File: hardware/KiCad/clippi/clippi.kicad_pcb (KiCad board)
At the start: 2 copper layers, 65 x 56 mm, 23 parts, among them J1 GPIO, J2 Conn_01x16_Pin, Q1 BSS138

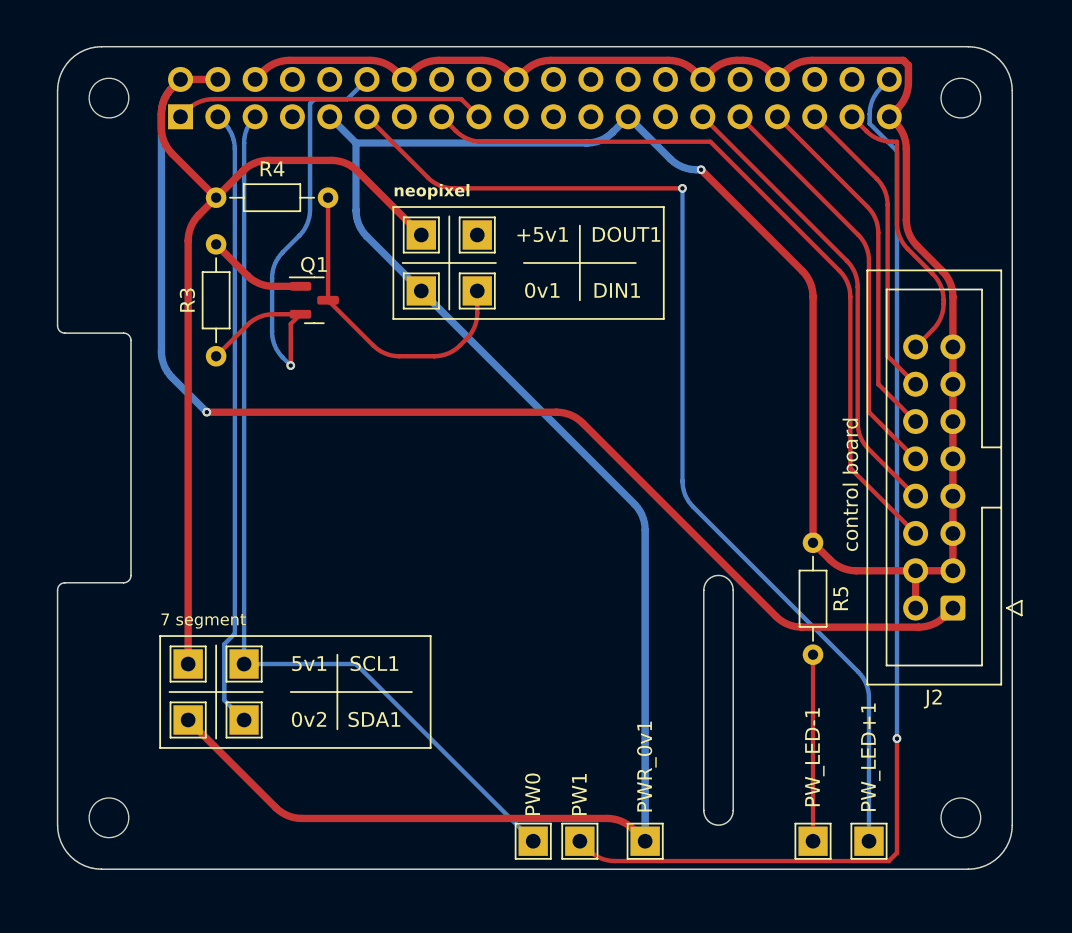
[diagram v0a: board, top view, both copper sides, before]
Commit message: re-lay out the pi hat, re-trace, add copper fill, and I generated gerber files and set it off to PCB way
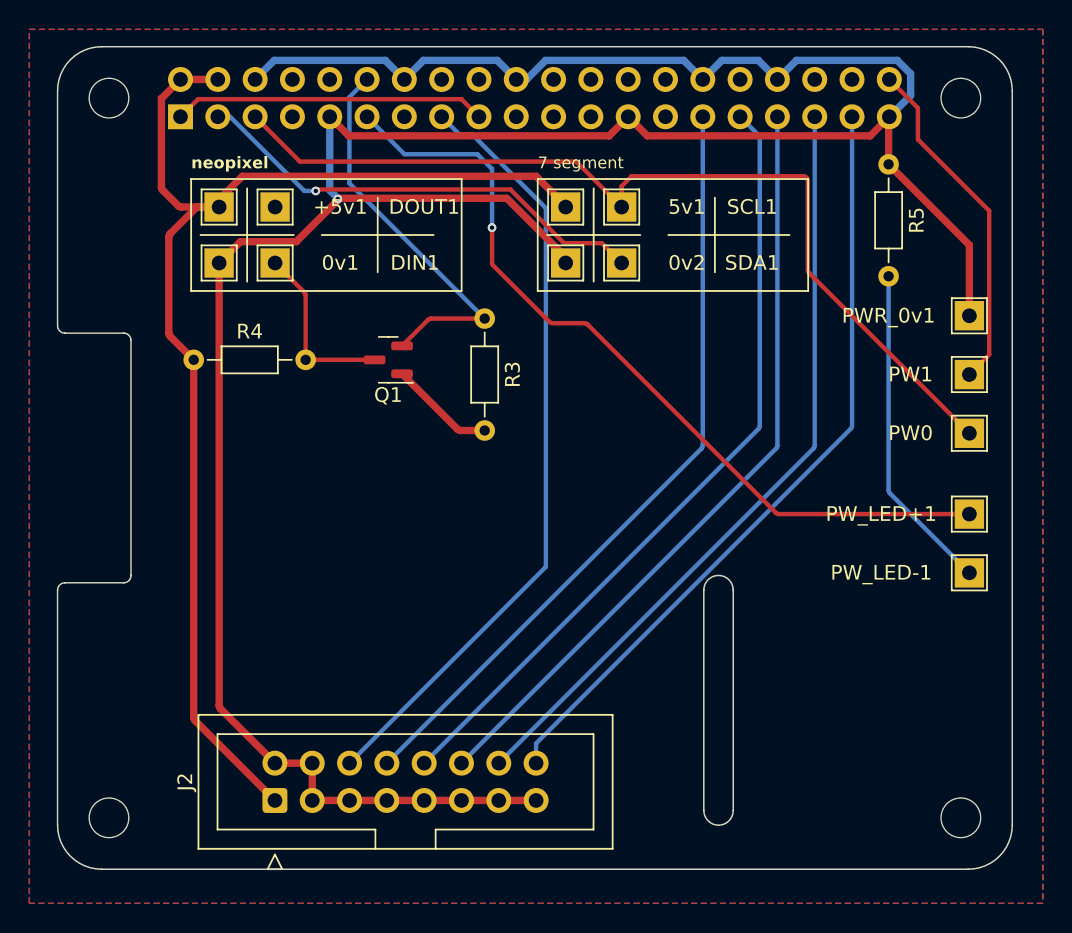
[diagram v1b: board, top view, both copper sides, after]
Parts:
- moved J2 48.0 mm to (114.8, 95.3), turned to 90 degrees
- moved PWR_0v1 42.0 mm to (162.1, 62.3)
- moved PW1 41.4 mm to (162.1, 66.3)
- moved PW0 40.7 mm to (162.1, 70.3)
- moved 0v2 40.4 mm to (134.6, 58.7)
- moved 5v1 40.4 mm to (134.6, 54.9)
- moved SCL1 40.4 mm to (138.4, 54.9)
- moved SDA1 40.4 mm to (138.4, 58.7)
- moved R5 26.3 mm to (156.6, 52.0)
- moved PW_LED+1 23.3 mm to (162.1, 75.8)
- moved PW_LED-1 21.1 mm to (162.1, 79.8)
- moved R3 18.5 mm to (129.1, 62.5), turned to -90 degrees
- moved +5v1 13.9 mm to (111.0, 54.9)
- moved 0v1 13.9 mm to (111.0, 58.7)
- moved DIN1 13.9 mm to (114.8, 58.7)
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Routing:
- net +5V: track 143.0 -> 86.3 mm, vias 1 -> 0
- net /GPIO21/PCM.DOUT: track 76.1 -> 23.5 mm, vias 1 -> 0
- net GND: track 243.6 -> 198.7 mm
- net /GPIO26: track 19.4 -> 52.9 mm
- net /GPIO19/PCM.FS: track 20.9 -> 52.9 mm
- net /GPIO13/PWM1: track 24.5 -> 52.9 mm
- net /GPIO6: track 28.1 -> 54.0 mm
- net /GPIO5: track 31.6 -> 52.9 mm
- net /GPIO17: track 72.8 -> 56.0 mm
- net /GPIO2/SDA1: track 42.3 -> 31.7 mm, vias 0 -> 1
- net Net-(PW_LED-1-Pin_1): track 12.7 -> 22.5 mm
- net /NPIXEL_DATA_IN: track 21.7 -> 12.1 mm
- net /GPIO18/PCM.CLK: track 34.2 -> 27.0 mm, vias 1 -> 0
- net /GPIO22: track 51.2 -> 53.0 mm
- net /GPIO3/SCL1: track 62.1 -> 63.8 mm
- added copper zone on B.Cu, net GND
- added copper zone on F.Cu, net GND
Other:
- board text removed: "control board"

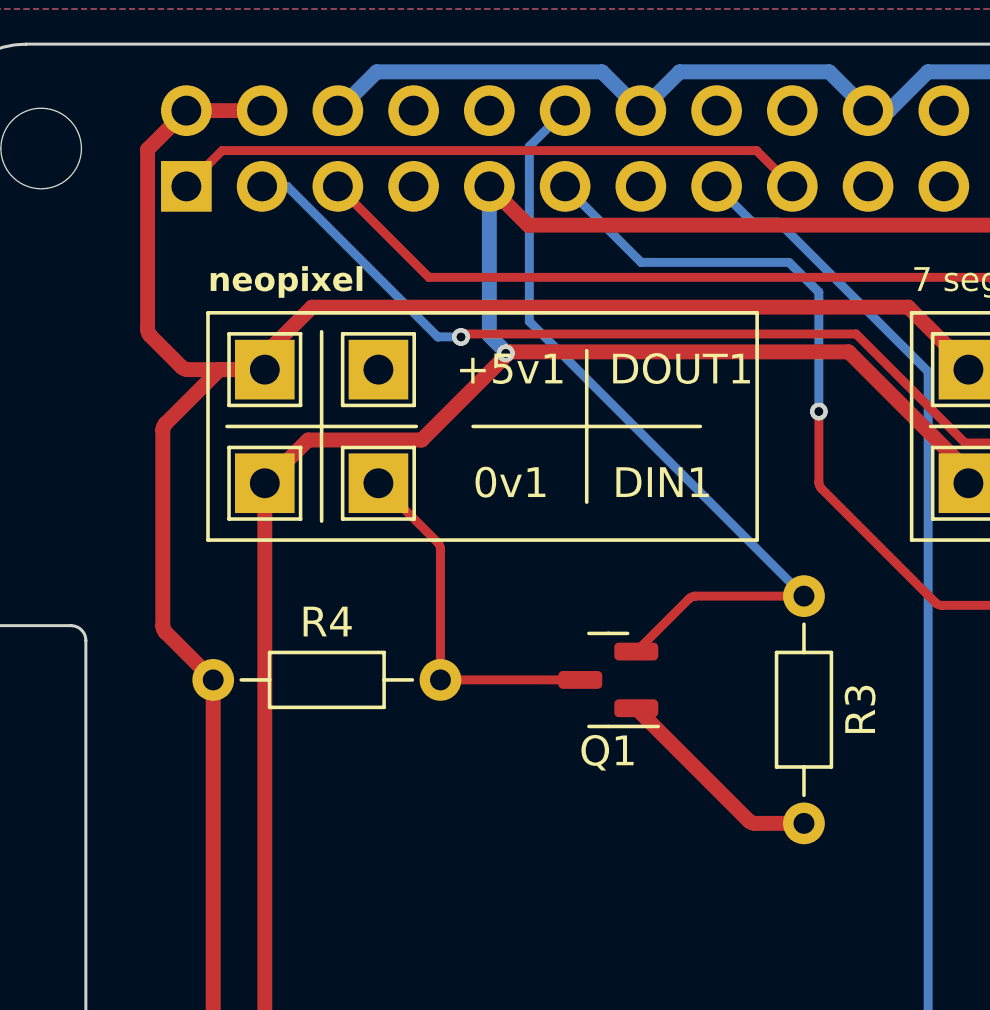
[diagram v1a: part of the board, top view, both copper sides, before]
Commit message: fix pi hat board/schematic to ensure 3.3v is supplied to the logic shifter, that got missed
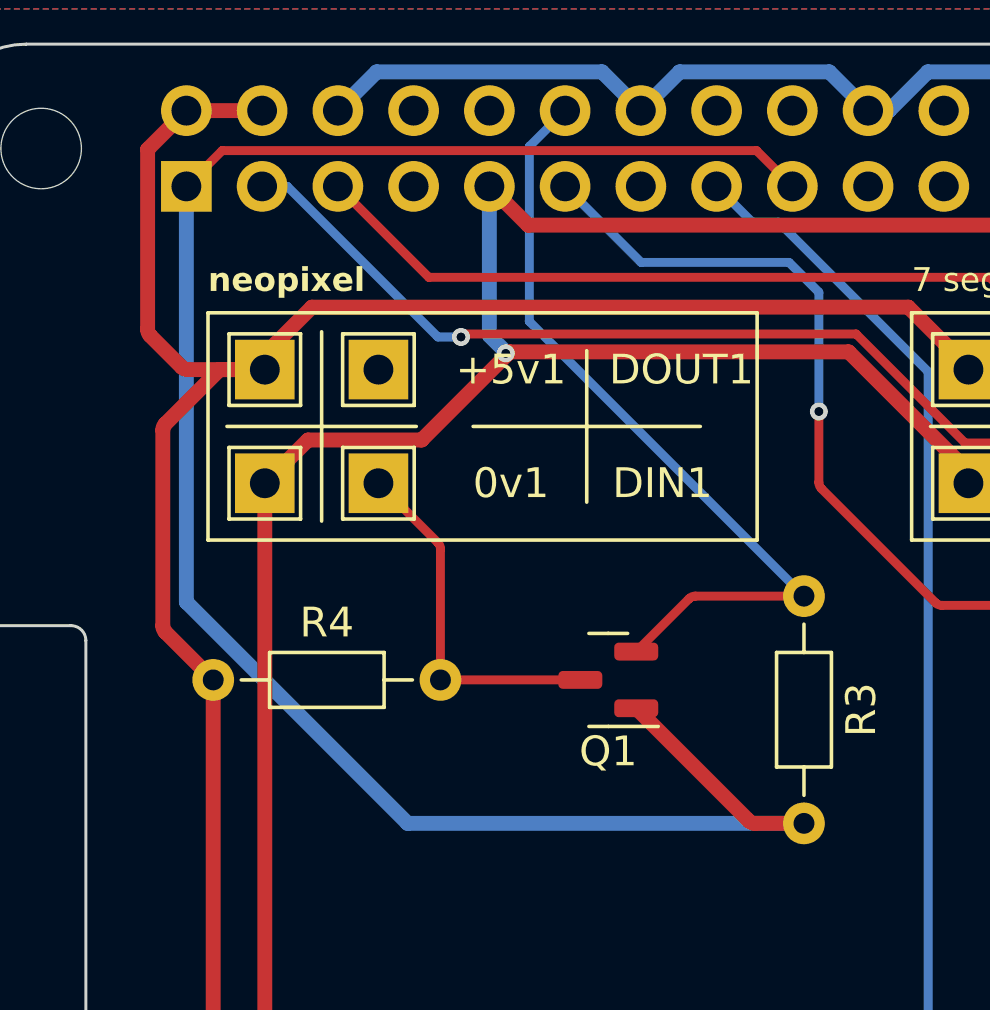
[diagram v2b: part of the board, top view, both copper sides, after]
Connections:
- Q1 pad 1: +3.3V -> +3V3
- R3 pad 2: +3.3V -> +3V3
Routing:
- net +3V3: track 21.3 -> 66.2 mm
- net +3.3V: track 7.21 -> 0.00 mm
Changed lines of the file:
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@@
   (net 33 "/NPIXEL_DATA_IN")
   (net 34 "/NPIXEL_DATA_OUT")
-  (net 35 "+3.3V")
   (footprint "MountingHole:MountingHole_2.7mm_M2.5" locked (layer "F.Cu")
     (at 161.5 47.5)
@@
       (net 8 "/GPIO18{slash}PCM.CLK") (pintype "passive"))
     (pad "2" thru_hole oval (at 7.62 0 270) (size 1.4 1.4) (drill 0.7) (layers "*.Cu" "*.Mask")
-      (net 35 "+3.3V") (pintype "passive"))
+      (net 31 "+3V3") (pintype "passive"))
     (model "${KICAD6_3DMODEL_DIR}/Resistor_THT.3dshapes/R_Axial_DIN0204_L3.6mm_D1.6mm_P7.62mm_Horizontal.wrl"
       (offset (xyz 0 0 0))
@@
       (stroke (width 0.1) (type solid)) (layer "F.Fab"))
     (pad "1" smd roundrect (at -0.9375 -0.95 180) (size 1.475 0.6) (layers "F.Cu" "F.Paste" "F.Mask") (roundrect_rratio 0.25)
-      (net 35 "+3.3V") (pinfunction "G") (pintype "input"))
+      (net 31 "+3V3") (pinfunction "G") (pintype "input"))
     (pad "2" smd roundrect (at -0.9375 0.95 180) (size 1.475 0.6) (layers "F.Cu" "F.Paste" "F.Mask") (roundrect_rratio 0.25)
       (net 8 "/GPIO18{slash}PCM.CLK") (pinfunction "S") (pintype "passive"))
@@
   (arc (start 107.157868 53.774163) (mid 107.092836 53.676836) (end 107.07 53.562031) (width 0.5) (layer "F.Cu") (net 30))
   (arc (start 109.357868 89.877868) (mid 109.292836 89.780541) (end 109.27 89.665736) (width 0.5) (layer "F.Cu") (net 30))
+  (segment (start 129.08 70.13) (end 127.439264 70.13) (width 0.5) (layer "F.Cu") (net 31))
   (segment (start 128.69 48.77) (end 127.49 47.57) (width 0.3) (layer "F.Cu") (net 31))
   (segment (start 127.49 47.57) (end 109.57 47.57) (width 0.3) (layer "F.Cu") (net 31))
   (segment (start 109.57 47.57) (end 108.37 48.77) (width 0.3) (layer "F.Cu") (net 31))
+  (segment (start 127.227132 70.042132) (end 123.455 66.27) (width 0.5) (layer "F.Cu") (net 31))
+  (arc (start 127.227132 70.042132) (mid 127.324459 70.107164) (end 127.439264 70.13) (width 0.5) (layer "F.Cu") (net 31))
+  (segment (start 129.08 70.13) (end 115.78826 70.13) (width 0.5) (layer "B.Cu") (net 31))
+  (segment (start 108.37 62.71174) (end 108.37 48.77) (width 0.5) (layer "B.Cu") (net 31))
+  (segment (start 115.78826 70.13) (end 108.37 62.71174) (width 0.5) (layer "B.Cu") (net 31))
   (segment (start 156.58 74.195736) (end 156.58 59.63) (width 0.3) (layer "B.Cu") (net 32))
   (segment (start 162.08 79.82) (end 156.667868 74.407868) (width 0.3) (layer "B.Cu") (net 32))
@@
   (segment (start 121.58 65.32) (end 116.89 65.32) (width 0.3) (layer "F.Cu") (net 33))
   (arc (start 116.89 60.929264) (mid 116.867164 60.814459) (end 116.802132 60.717132) (width 0.3) (layer "F.Cu") (net 33))
-  (segment (start 129.08 70.13) (end 127.439264 70.13) (width 0.5) (layer "F.Cu") (net 35))
-  (segment (start 127.227132 70.042132) (end 123.455 66.27) (width 0.5) (layer "F.Cu") (net 35))
-  (arc (start 127.227132 70.042132) (mid 127.324459 70.107164) (end 127.439264 70.13) (width 0.5) (layer "F.Cu") (net 35))
   (zone (net 1) (net_name "GND") (layers "F&B.Cu") (hatch edge 0.5)
     (connect_pads (clearance 0))
